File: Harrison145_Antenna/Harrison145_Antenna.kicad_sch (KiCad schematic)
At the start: 13 parts, among them J1 Conn_01x01, J2 Conn_01x01, J3 AudioJack3, SW1 SW_SPDT

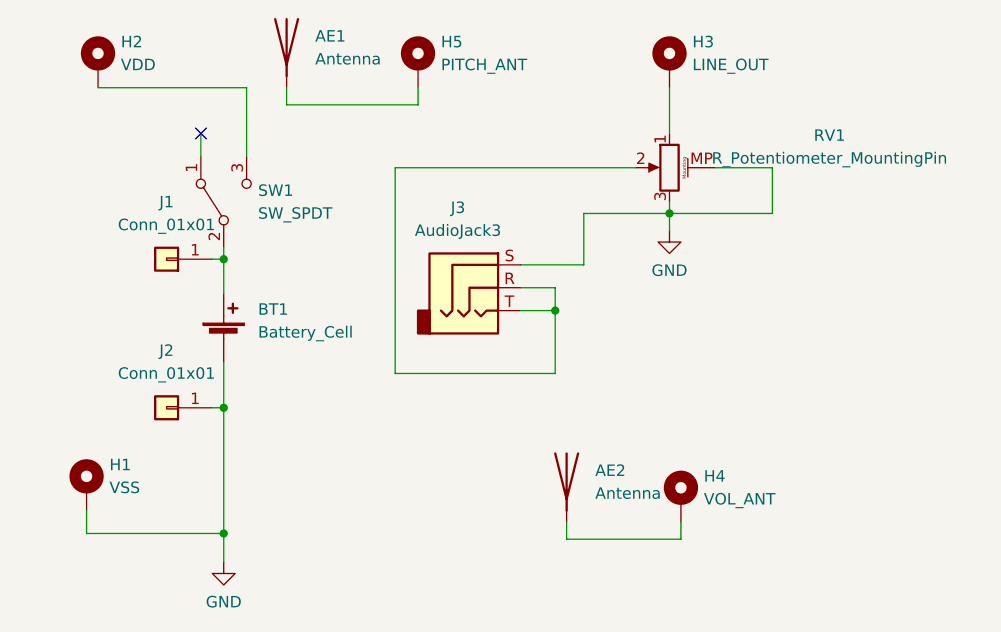
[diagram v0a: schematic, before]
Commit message: Antenna design changes
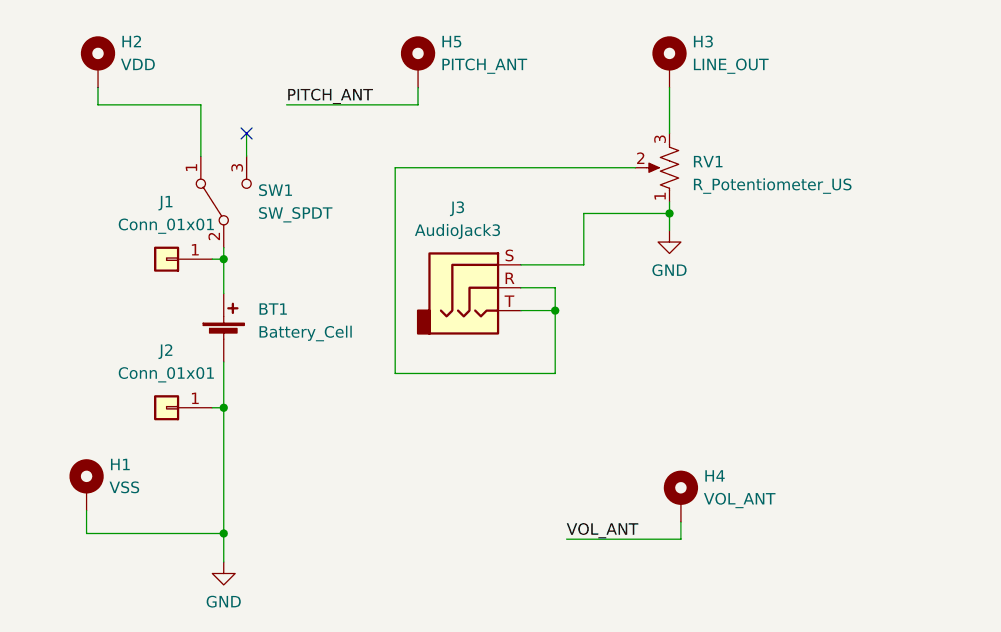
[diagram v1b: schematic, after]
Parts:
- removed AE1: Antenna, symbol Device:Antenna
- removed AE2: Antenna, Theremin:PlateAntenna, symbol Device:Antenna
- removed RV1: R_Potentiometer_MountingPin, Theremin:PTV09A3015FB103, symbol Device:R_Potentiometer_MountingPin
- added RV1: R_Potentiometer_US, Theremin:PTV09A3015FB103, symbol Device:R_Potentiometer_US
- BT1: now left out of the parts list
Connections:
- net GND: now also RV1.1
- net PITCH_ANT: now reaches H5.1
- net VOL_ANT: now reaches H4.1
- net at J3.R, J3.T: now also RV1.2
- net at H3.1: now also RV1.3
- net at SW1.1 (A): now also H2.1
- net at SW1.3 (C): no longer H2.1

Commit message: Combine 9V battery and terminals into a single footprint
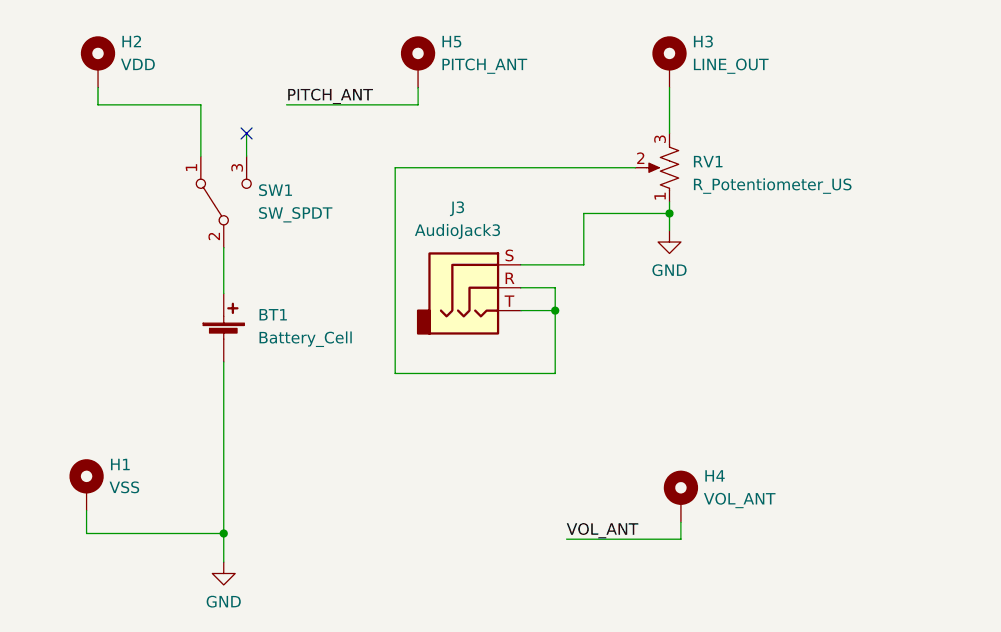
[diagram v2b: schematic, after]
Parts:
- removed J1: Conn_01x01, Theremin:Keystone_594, symbol Connector_Generic:Conn_01x01
- removed J2: Conn_01x01, Theremin:Keystone_593, symbol Connector_Generic:Conn_01x01
- BT1: now in the parts list
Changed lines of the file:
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@@
 (kicad_sch (version 20221206) (generator eeschema)
   (paper "A4")
-  (junction (at 81.28 66.04) (diameter 0) (color 0 0 0 0)
-  )
   (junction (at 81.28 80.01) (diameter 0) (color 0 0 0 0)
-  )
-  (junction (at 81.28 49.53) (diameter 0) (color 0 0 0 0)
   )
   (junction (at 130.81 44.45) (diameter 0) (color 0 0 0 0)
@@
     (stroke (width 0) (type default))
   )
-  (wire (pts (xy 81.28 48.26) (xy 81.28 49.53))
-    (stroke (width 0) (type default))
-  )
   (wire (pts (xy 114.3 52.705) (xy 118.11 52.705))
     (stroke (width 0) (type default))
   )
-  (wire (pts (xy 81.28 60.96) (xy 81.28 66.04))
-    (stroke (width 0) (type default))
-  )
   (wire (pts (xy 100.33 62.23) (xy 118.11 62.23))
     (stroke (width 0) (type default))
@@
     (stroke (width 0) (type default))
   )
-  (wire (pts (xy 81.28 49.53) (xy 81.28 53.34))
+  (wire (pts (xy 81.28 48.26) (xy 81.28 53.34))
     (stroke (width 0) (type default))
   )
@@
     (stroke (width 0) (type default))
   )
-  (wire (pts (xy 80.01 49.53) (xy 81.28 49.53))
-    (stroke (width 0) (type default))
-  )
   (wire (pts (xy 66.04 80.01) (xy 81.28 80.01))
     (stroke (width 0) (type default))
@@
     (stroke (width 0) (type default))
   )
-  (wire (pts (xy 81.28 66.04) (xy 81.28 80.01))
+  (wire (pts (xy 81.28 60.96) (xy 81.28 80.01))
     (stroke (width 0) (type default))
   )
@@
   )
   (wire (pts (xy 119.38 80.645) (xy 132.08 80.645))
-    (stroke (width 0) (type default))
-  )
-  (wire (pts (xy 80.01 66.04) (xy 81.28 66.04))
     (stroke (width 0) (type default))
   )
@@
   (label "PITCH_ANT" (at 88.265 32.385 0) (fields_autoplaced)
     (effects (font (size 1.27 1.27)) (justify left bottom))
-  )
-  (symbol (lib_id "Device:Battery_Cell") (at 81.28 58.42 0) (unit 1)
-    (in_bom no) (on_board yes) (dnp no) (fields_autoplaced)
-    (property "Reference" "BT1" (at 85.09 55.1179 0)
-      (effects (font (size 1.27 1.27)) (justify left))
-    )
-    (property "Value" "Battery_Cell" (at 85.09 57.6579 0)
-      (effects (font (size 1.27 1.27)) (justify left))
-    )
-    (property "Footprint" "Theremin:9V_Bat" (at 81.28 56.896 90)
-      (effects (font (size 1.27 1.27)) hide)
-    )
-    (property "Datasheet" "~" (at 81.28 56.896 90)
-      (effects (font (size 1.27 1.27)) hide)
-    )
-    (pin "1")
-    (pin "2")
-    (instances
-      (project "Harrison145_Antenna"
-        (path "/fe6a253a-fbe7-4763-8fb6-20765e8d5d9d"
-          (reference "BT1") (unit 1)
-        )
-      )
-    )
   )
   (symbol (lib_id "Mechanical:MountingHole_Pad") (at 132.08 76.2 0) (unit 1)
@@
     )
   )
-  (symbol (lib_id "Connector_Generic:Conn_01x01") (at 74.93 49.53 180) (unit 1)
-    (in_bom yes) (on_board yes) (dnp no) (fields_autoplaced)
-    (property "Reference" "J1" (at 74.93 43.18 0)
-      (effects (font (size 1.27 1.27)))
-    )
-    (property "Value" "Conn_01x01" (at 74.93 45.72 0)
-      (effects (font (size 1.27 1.27)))
-    )
-    (property "Footprint" "Theremin:Keystone_594" (at 74.93 49.53 0)
-      (effects (font (size 1.27 1.27)) hide)
-    )
-    (property "Datasheet" "~" (at 74.93 49.53 0)
-      (effects (font (size 1.27 1.27)) hide)
-    )
-    (pin "1")
-    (instances
-      (project "Harrison145_Antenna"
-        (path "/fe6a253a-fbe7-4763-8fb6-20765e8d5d9d"
-          (reference "J1") (unit 1)
-        )
-      )
-    )
-  )
-  (symbol (lib_id "Connector_Generic:Conn_01x01") (at 74.93 66.04 180) (unit 1)
-    (in_bom yes) (on_board yes) (dnp no) (fields_autoplaced)
-    (property "Reference" "J2" (at 74.93 59.69 0)
-      (effects (font (size 1.27 1.27)))
-    )
-    (property "Value" "Conn_01x01" (at 74.93 62.23 0)
-      (effects (font (size 1.27 1.27)))
-    )
-    (property "Footprint" "Theremin:Keystone_593" (at 74.93 66.04 0)
-      (effects (font (size 1.27 1.27)) hide)
-    )
-    (property "Datasheet" "~" (at 74.93 66.04 0)
-      (effects (font (size 1.27 1.27)) hide)
-    )
-    (pin "1")
-    (instances
-      (project "Harrison145_Antenna"
-        (path "/fe6a253a-fbe7-4763-8fb6-20765e8d5d9d"
-          (reference "J2") (unit 1)
-        )
-      )
+  (symbol (lib_id "Device:Battery_Cell") (at 81.28 58.42 0) (unit 1)
+    (in_bom yes) (on_board yes) (dnp no) (fields_autoplaced)
+    (property "Reference" "BT1" (at 85.09 55.753 0)
+      (effects (font (size 1.27 1.27)) (justify left))
+    )
+    (property "Value" "Battery_Cell" (at 85.09 58.293 0)
+      (effects (font (size 1.27 1.27)) (justify left))
+    )
+    (property "Footprint" "Theremin:9V_Bat" (at 81.28 56.896 90)
+      (effects (font (size 1.27 1.27)) hide)
+    )
+    (property "Datasheet" "~" (at 81.28 56.896 90)
+      (effects (font (size 1.27 1.27)) hide)
+    )
+    (pin "1")
+    (pin "2")
+    (instances
+      (project "Harrison145_Antenna"
+        (path "/fe6a253a-fbe7-4763-8fb6-20765e8d5d9d"
+          (reference "BT1") (unit 1)
+        )
+      )

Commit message: Cutouts on antenna pcb
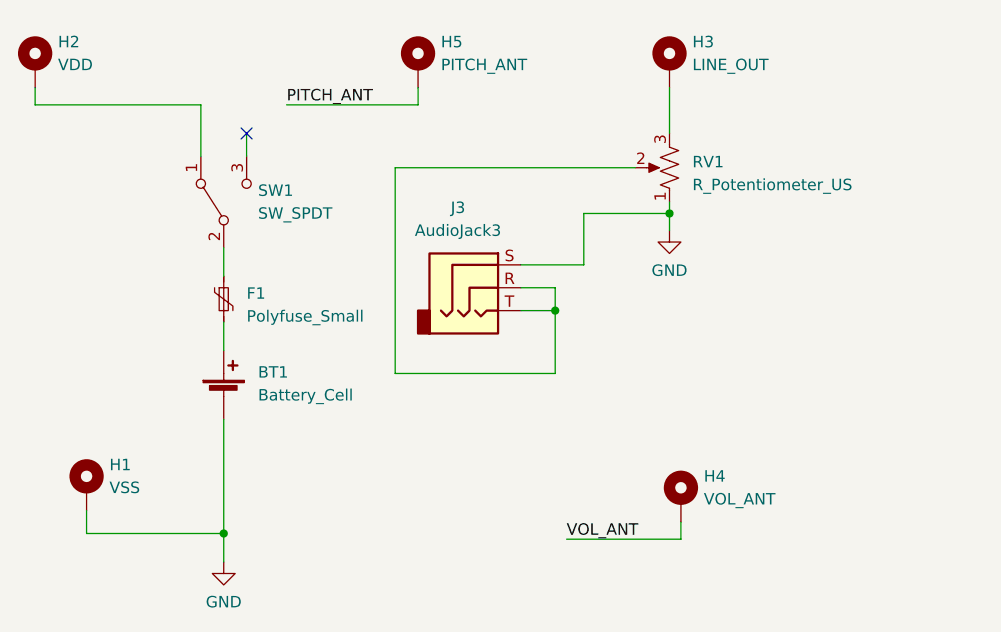
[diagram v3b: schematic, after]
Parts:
- added F1: Polyfuse_Small, Fuse:Fuse_1812_4532Metric_Pad1.30x3.40mm_HandSolder, symbol Device:Polyfuse_Small
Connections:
- net at BT1.1 (+): now also F1.2; no longer SW1.2 (B)
- new net: F1.1, SW1.2 (B)
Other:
- moved on the sheet: BT1, H2
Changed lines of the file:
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@@
     (stroke (width 0) (type default))
   )
-  (wire (pts (xy 67.31 30.48) (xy 67.31 32.385))
+  (wire (pts (xy 60.325 30.48) (xy 60.325 32.385))
     (stroke (width 0) (type default))
   )
@@
     (stroke (width 0) (type default))
   )
-  (wire (pts (xy 78.74 32.385) (xy 67.31 32.385))
-    (stroke (width 0) (type default))
-  )
   (wire (pts (xy 81.28 80.01) (xy 81.28 83.185))
     (stroke (width 0) (type default))
@@
     (stroke (width 0) (type default))
   )
-  (wire (pts (xy 81.28 48.26) (xy 81.28 53.34))
+  (wire (pts (xy 81.28 59.69) (xy 81.28 56.515))
     (stroke (width 0) (type default))
   )
@@
     (stroke (width 0) (type default))
   )
+  (wire (pts (xy 60.325 32.385) (xy 78.74 32.385))
+    (stroke (width 0) (type default))
+  )
   (wire (pts (xy 118.11 55.245) (xy 118.11 62.23))
     (stroke (width 0) (type default))
   )
-  (wire (pts (xy 81.28 60.96) (xy 81.28 80.01))
+  (wire (pts (xy 81.28 51.435) (xy 81.28 48.26))
+    (stroke (width 0) (type default))
+  )
+  (wire (pts (xy 81.28 67.31) (xy 81.28 80.01))
     (stroke (width 0) (type default))
   )
@@
     )
   )
-  (symbol (lib_id "Device:Battery_Cell") (at 81.28 58.42 0) (unit 1)
-    (in_bom yes) (on_board yes) (dnp no) (fields_autoplaced)
-    (property "Reference" "BT1" (at 85.09 55.753 0)
-      (effects (font (size 1.27 1.27)) (justify left))
-    )
-    (property "Value" "Battery_Cell" (at 85.09 58.293 0)
-      (effects (font (size 1.27 1.27)) (justify left))
-    )
-    (property "Footprint" "Theremin:9V_Bat" (at 81.28 56.896 90)
-      (effects (font (size 1.27 1.27)) hide)
-    )
-    (property "Datasheet" "~" (at 81.28 56.896 90)
+  (symbol (lib_id "Device:Battery_Cell") (at 81.28 64.77 0) (unit 1)
+    (in_bom yes) (on_board yes) (dnp no) (fields_autoplaced)
+    (property "Reference" "BT1" (at 85.09 62.103 0)
+      (effects (font (size 1.27 1.27)) (justify left))
+    )
+    (property "Value" "Battery_Cell" (at 85.09 64.643 0)
+      (effects (font (size 1.27 1.27)) (justify left))
+    )
+    (property "Footprint" "Theremin:9V_Bat" (at 81.28 63.246 90)
+      (effects (font (size 1.27 1.27)) hide)
+    )
+    (property "Datasheet" "~" (at 81.28 63.246 90)
       (effects (font (size 1.27 1.27)) hide)
     )
@@
     )
   )
+  (symbol (lib_id "Device:Polyfuse_Small") (at 81.28 53.975 0) (unit 1)
+    (in_bom yes) (on_board yes) (dnp no) (fields_autoplaced)
+    (property "Reference" "F1" (at 83.82 53.34 0)
+      (effects (font (size 1.27 1.27)) (justify left))
+    )
+    (property "Value" "Polyfuse_Small" (at 83.82 55.88 0)
+      (effects (font (size 1.27 1.27)) (justify left))
+    )
+    (property "Footprint" "Fuse:Fuse_1812_4532Metric_Pad1.30x3.40mm_HandSolder" (at 82.55 59.055 0)
+      (effects (font (size 1.27 1.27)) (justify left) hide)
+    )
+    (property "Datasheet" "~" (at 81.28 53.975 0)
+      (effects (font (size 1.27 1.27)) hide)
+    )
+    (pin "1")
+    (pin "2")
+    (instances
+      (project "Harrison145_Antenna"
+        (path "/fe6a253a-fbe7-4763-8fb6-20765e8d5d9d"
+          (reference "F1") (unit 1)
+        )
+      )
+    )
+  )
   (symbol (lib_id "Switch:SW_SPDT") (at 81.28 43.18 90) (unit 1)
     (in_bom yes) (on_board yes) (dnp no) (fields_autoplaced)
@@
     )
   )
-  (symbol (lib_id "Mechanical:MountingHole_Pad") (at 67.31 27.94 0) (unit 1)
-    (in_bom yes) (on_board yes) (dnp no) (fields_autoplaced)
-    (property "Reference" "H2" (at 69.85 25.3999 0)
-      (effects (font (size 1.27 1.27)) (justify left))
-    )
-    (property "Value" "VDD" (at 69.85 27.9399 0)
-      (effects (font (size 1.27 1.27)) (justify left))
-    )
-    (property "Footprint" "Theremin:SMTSO-M4" (at 67.31 27.94 0)
-      (effects (font (size 1.27 1.27)) hide)
-    )
-    (property "Datasheet" "~" (at 67.31 27.94 0)
-      (effects (font (size 1.27 1.27)) hide)
-    )
+  (symbol (lib_id "Mechanical:MountingHole_Pad") (at 60.325 27.94 0) (unit 1)
+    (in_bom yes) (on_board yes) (dnp no) (fields_autoplaced)
+    (property "Reference" "H2" (at 62.865 25.3999 0)
+      (effects (font (size 1.27 1.27)) (justify left))
+    )
+    (property "Value" "VDD" (at 62.865 27.9399 0)
+      (effects (font (size 1.27 1.27)) (justify left))
+    )
+    (property "Footprint" "Theremin:SMTSO-M4" (at 60.325 27.94 0)
+      (effects (font (size 1.27 1.27)) hide)
+    )
+    (property "Datasheet" "~" (at 60.325 27.94 0)
+      (effects (font (size 1.27 1.27)) hide)
+    )
